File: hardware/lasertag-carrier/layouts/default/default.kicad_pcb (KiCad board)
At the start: 2 copper layers, 100 x 80 mm, 39 parts, among them J0 Power in 2P, J1 S3-Matrix L, J12 Ext button, J13 Touch hdr, J14 Activity LED, J2 S3-Matrix R, J3 MAX98357A, J4 Speaker, J5 microSD, J6 IR RX, J7 IR LED, J8 WS2812 out, J9 OLED I2C, Q1 2N2222A, SW1 SW_PUSH_6mm, SW2 PWR switch

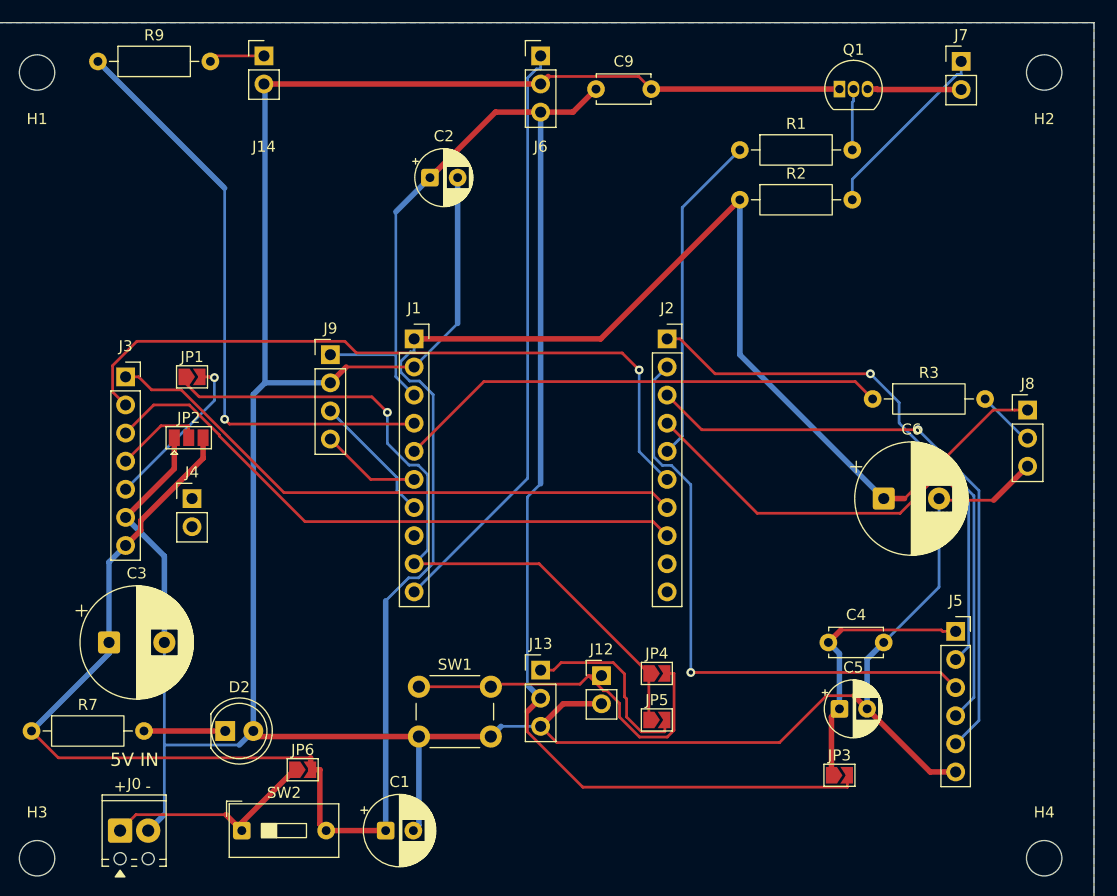
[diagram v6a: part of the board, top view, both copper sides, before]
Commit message: Silk: pin-1 signal labels on all connectors; regenerate fab package
- pin-1 labels: 5V (J1), LRC (J3), 3V3 (J5), SIG (J13)
- full pin labels: OUT/GND/3V3 (J6), 5V/DAT/GND (J8), 3V3/GND/SDA/SCL (J9)
- polarity marks: J0 "+" -> "+5V", +/- added to J4 speaker and both LED
  headers J7/J14 (their Value text lives on F.Fab, which never prints)
- all label text at 0.8mm (board min); J3/J5/J13/J6 refdes relocated clear
- one known-phantom silk_overlap warning remains (kicad-cli 10.0.3 pairs
  J6's ref with a segment 7mm away; persists through moves and hide, silk
  Gerber verified correct by inspection)
- fab zip regenerated with the new silkscreen

Co-Authored-By: Claude Opus 4.8 <noreply@anthropic.com>
Claude-Session: https://claude.ai/code/session_01TutNLcDSScdeeVSbjpyg8j
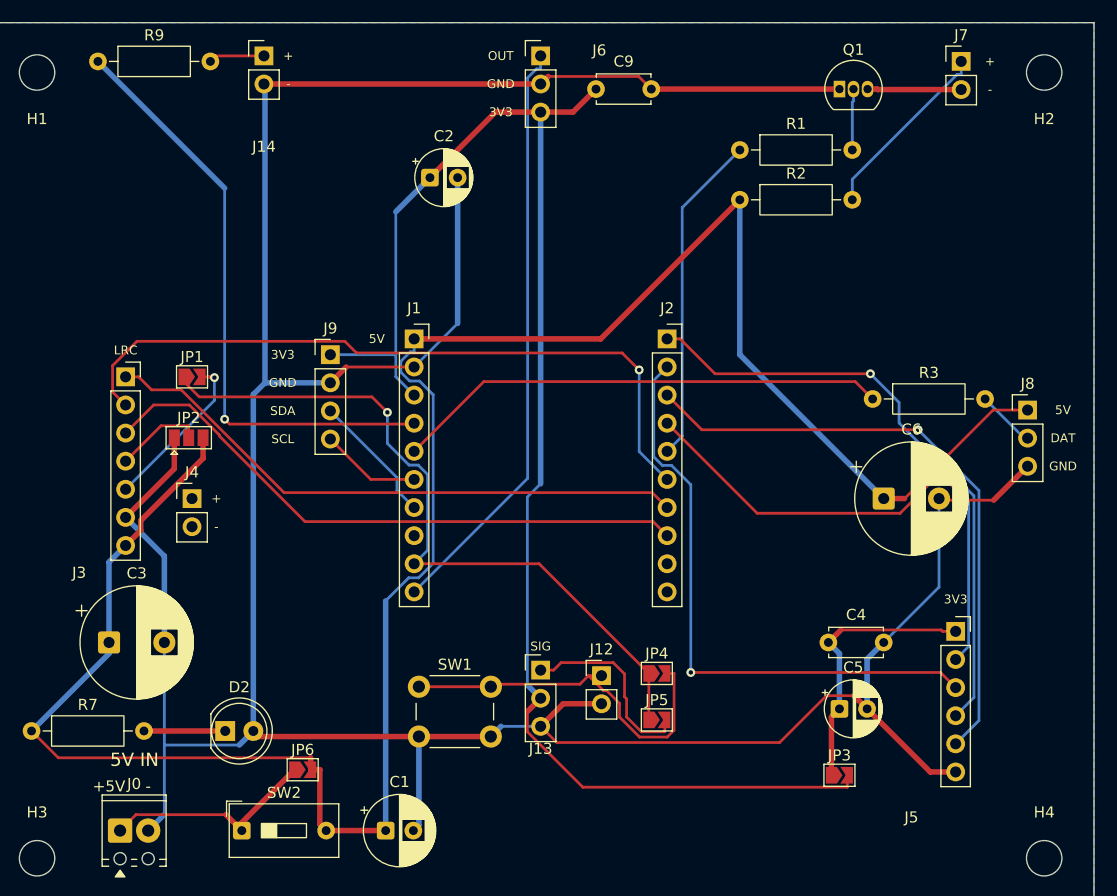
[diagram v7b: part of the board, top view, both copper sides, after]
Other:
- board text added: "+5V"
- board text added: "3V3"
- board text added: "5V"
- board text added: "DAT"
- board text added: "GND"
- board text added: "LRC"
- board text added: "OUT"
- board text added: "SCL"
- board text added: "SDA"
- board text added: "SIG"
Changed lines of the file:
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@@
 		(at 150 118.5)
 		(property "Reference" "J13"
-			(at 0 -2.38 0)
+			(at 0 7.1 0)
 			(layer "F.SilkS")
 			(effects
@@
 		(at 187.5 115)
 		(property "Reference" "J5"
-			(at 0 -2.77 0)
+			(at -4 16.8 0)
 			(layer "F.SilkS")
 			(effects
@@
 		(at 112.5 92)
 		(property "Reference" "J3"
-			(at 0 -2.77 0)
+			(at -4.2 17.7 0)
 			(layer "F.SilkS")
 			(effects
@@
 		(at 150 63)
 		(property "Reference" "J6"
-			(at 0 8.2 0)
+			(at 5.3 -0.5 0)
 			(layer "F.SilkS")
 			(effects
@@
 		(layer "Edge.Cuts")
 	)
+	(gr_text "LRC"
+		(at 112.5 89.6 0)
+		(layer "F.SilkS")
+		(effects
+			(font
+				(size 0.8 0.8)
+				(thickness 0.128)
+			)
+		)
+	)
 	(gr_text "+"
-		(at 112 129 0)
+		(at 120.7 103 0)
+		(layer "F.SilkS")
+		(effects
+			(font
+				(size 0.8 0.8)
+				(thickness 0.128)
+			)
+		)
+	)
+	(gr_text "-"
+		(at 120.7 105.54 0)
+		(layer "F.SilkS")
+		(effects
+			(font
+				(size 0.8 0.8)
+				(thickness 0.128)
+			)
+		)
+	)
+	(gr_text "+"
+		(at 127.2 63 0)
+		(layer "F.SilkS")
+		(effects
+			(font
+				(size 0.8 0.8)
+				(thickness 0.128)
+			)
+		)
+	)
+	(gr_text "-"
+		(at 127.2 65.54 0)
+		(layer "F.SilkS")
+		(effects
+			(font
+				(size 0.8 0.8)
+				(thickness 0.128)
+			)
+		)
+	)
+	(gr_text "5V"
+		(at 135.2 88.57 0)
+		(layer "F.SilkS")
+		(effects
+			(font
+				(size 0.8 0.8)
+				(thickness 0.128)
+			)
+		)
+	)
+	(gr_text "3V3"
+		(at 187.5 112.1 0)
+		(layer "F.SilkS")
+		(effects
+			(font
+				(size 0.8 0.8)
+				(thickness 0.128)
+			)
+		)
+	)
+	(gr_text "+"
+		(at 190.6 63.5 0)
+		(layer "F.SilkS")
+		(effects
+			(font
+				(size 0.8 0.8)
+				(thickness 0.128)
+			)
+		)
+	)
+	(gr_text "-"
+		(at 190.6 66.04 0)
+		(layer "F.SilkS")
+		(effects
+			(font
+				(size 0.8 0.8)
+				(thickness 0.128)
+			)
+		)
+	)
+	(gr_text "+5V"
+		(at 111 129 0)
 		(layer "F.SilkS")
 		(effects
@@
 	)
 	(embedded_fonts no)
+	(gr_text "OUT"
+		(at 146.4 63.0 0)
+		(layer "F.SilkS")
+		(effects
+			(font
+				(size 0.8 0.8)
+				(thickness 0.13)
+			)
+		)
+	)
+	(gr_text "GND"
+		(at 146.4 65.54 0)
+		(layer "F.SilkS")
+		(effects
+			(font
+				(size 0.8 0.8)
+				(thickness 0.13)
+			)
+		)
+	)
+	(gr_text "3V3"
+		(at 146.4 68.08 0)
+		(layer "F.SilkS")
+		(effects
+			(font
+				(size 0.8 0.8)
+				(thickness 0.13)
+			)
+		)
+	)
+	(gr_text "5V"
+		(at 197.2 95.0 0)
+		(layer "F.SilkS")
+		(effects
+			(font
+				(size 0.8 0.8)
+				(thickness 0.13)
+			)
+		)
+	)
+	(gr_text "DAT"
+		(at 197.2 97.54 0)
+		(layer "F.SilkS")
+		(effects
+			(font
+				(size 0.8 0.8)
+				(thickness 0.13)
+			)
+		)
+	)
+	(gr_text "GND"
+		(at 197.2 100.08 0)
+		(layer "F.SilkS")
+		(effects
+			(font
+				(size 0.8 0.8)
+				(thickness 0.13)
+			)
+		)
+	)
+	(gr_text "3V3"
+		(at 126.7 90.0 0)
+		(layer "F.SilkS")
+		(effects
+			(font
+				(size 0.8 0.8)
+				(thickness 0.13)
+			)
+		)
+	)
+	(gr_text "GND"
+		(at 126.7 92.54 0)
+		(layer "F.SilkS")
+		(effects
+			(font
+				(size 0.8 0.8)
+				(thickness 0.13)
+			)
+		)
+	)
+	(gr_text "SDA"
+		(at 126.7 95.08 0)
+		(layer "F.SilkS")
+		(effects
+			(font
+				(size 0.8 0.8)
+				(thickness 0.13)
+			)
+		)
+	)
+	(gr_text "SCL"
+		(at 126.7 97.62 0)
+		(layer "F.SilkS")
+		(effects
+			(font
+				(size 0.8 0.8)
+				(thickness 0.13)
+			)
+		)
+	)
+	(gr_text "SIG"
+		(at 150.0 116.35 0)
+		(layer "F.SilkS")
+		(effects
+			(font
+				(size 0.8 0.8)
+				(thickness 0.13)
+			)
+		)
+	)
 )

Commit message: Rotate IR receiver header J6 horizontal: OUT left, 3V3 right
The receiver bends up/down more naturally than sideways. J6 now runs
along the top edge with pads at (146.5/149.04/151.58, 63): pin 1 (OUT,
square pad) on the left, GND centre, 3V3 right; labels moved under each
pin and the refdes to the left of the body.

Reroute: removed the 9 orphaned segments from the old vertical position
(connectivity-verified iterative sweep), rerouted via Freerouting (J6's
GND pad is served by the B.Cu pour), re-ran the widen/narrow DRC guard.

DRC: 0 unconnected, 0 electrical; the single known-phantom silk_overlap
warning remains (it re-pairs J6's ref with whatever segment regardless of
position - kicad-cli 10.0.3 bug, silk Gerber verified correct).

Fab zip regenerated - use this one for PCBWay.

Co-Authored-By: Claude Opus 4.8 <noreply@anthropic.com>
Claude-Session: https://claude.ai/code/session_01TutNLcDSScdeeVSbjpyg8j
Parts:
- moved J6 3.50 mm to (146.5, 63.0), turned to 90 degrees
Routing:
- net VCC3V3: track 135.4 -> 143.2 mm
- net ir_rx: track 53.4 -> 56.0 mm, vias 0 -> 1
- net VCC5_IN: track 19.5 -> 21.0 mm
